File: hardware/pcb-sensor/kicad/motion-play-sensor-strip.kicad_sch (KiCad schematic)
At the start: 8 parts, among them J1 Power In, J2 Power Out, J3 I2C+INT, U1 VCNL4040M3OE-H3, U2 VCNL4040M3OE-H3

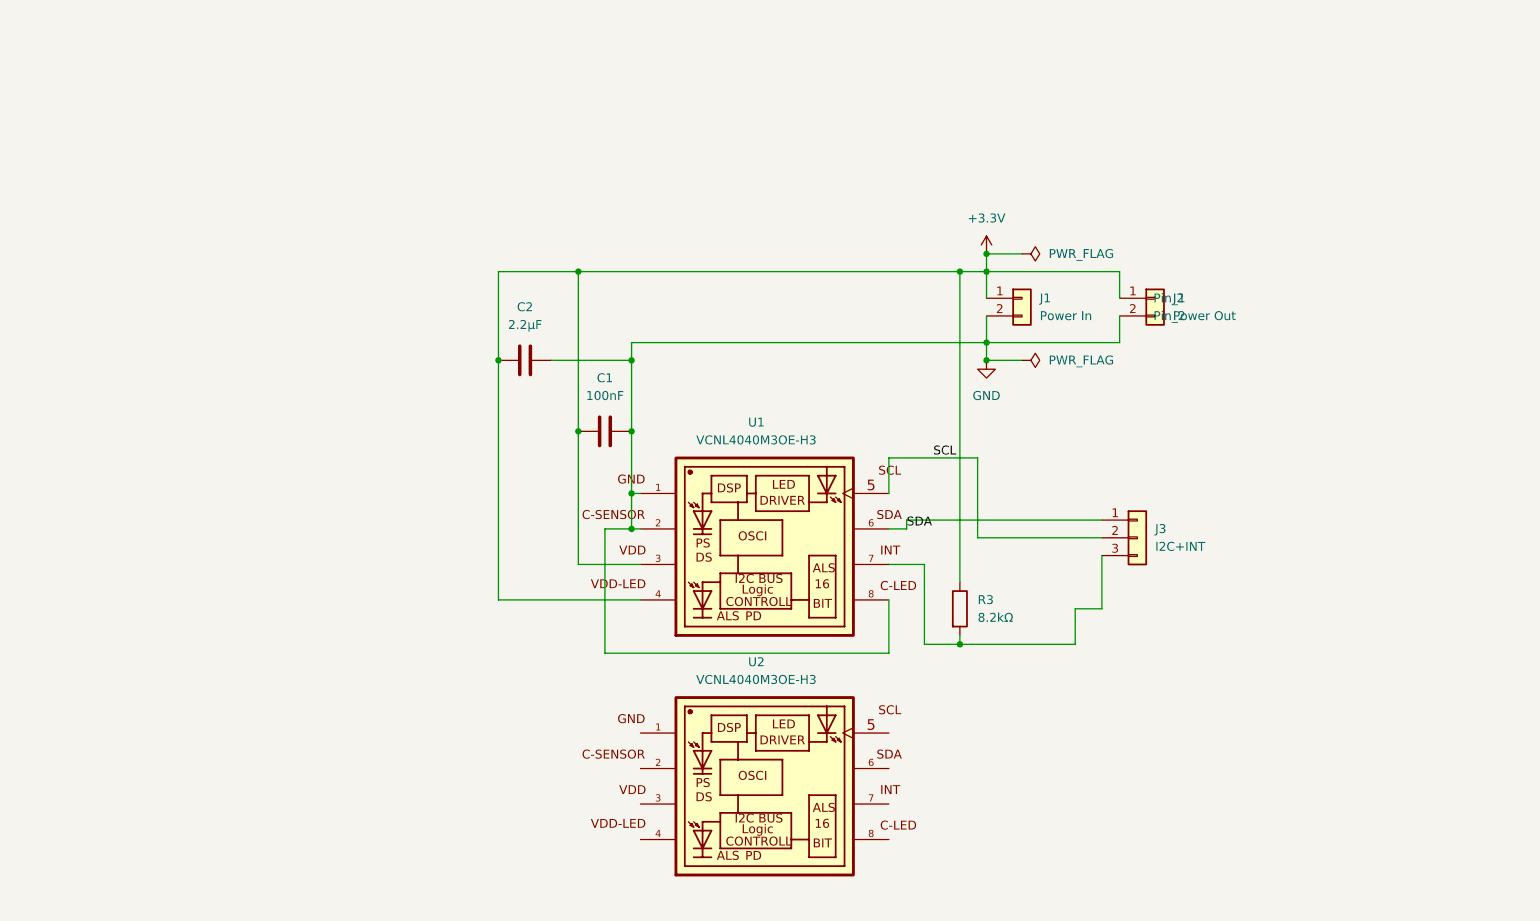
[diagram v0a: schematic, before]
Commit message: Finished sensor redesign
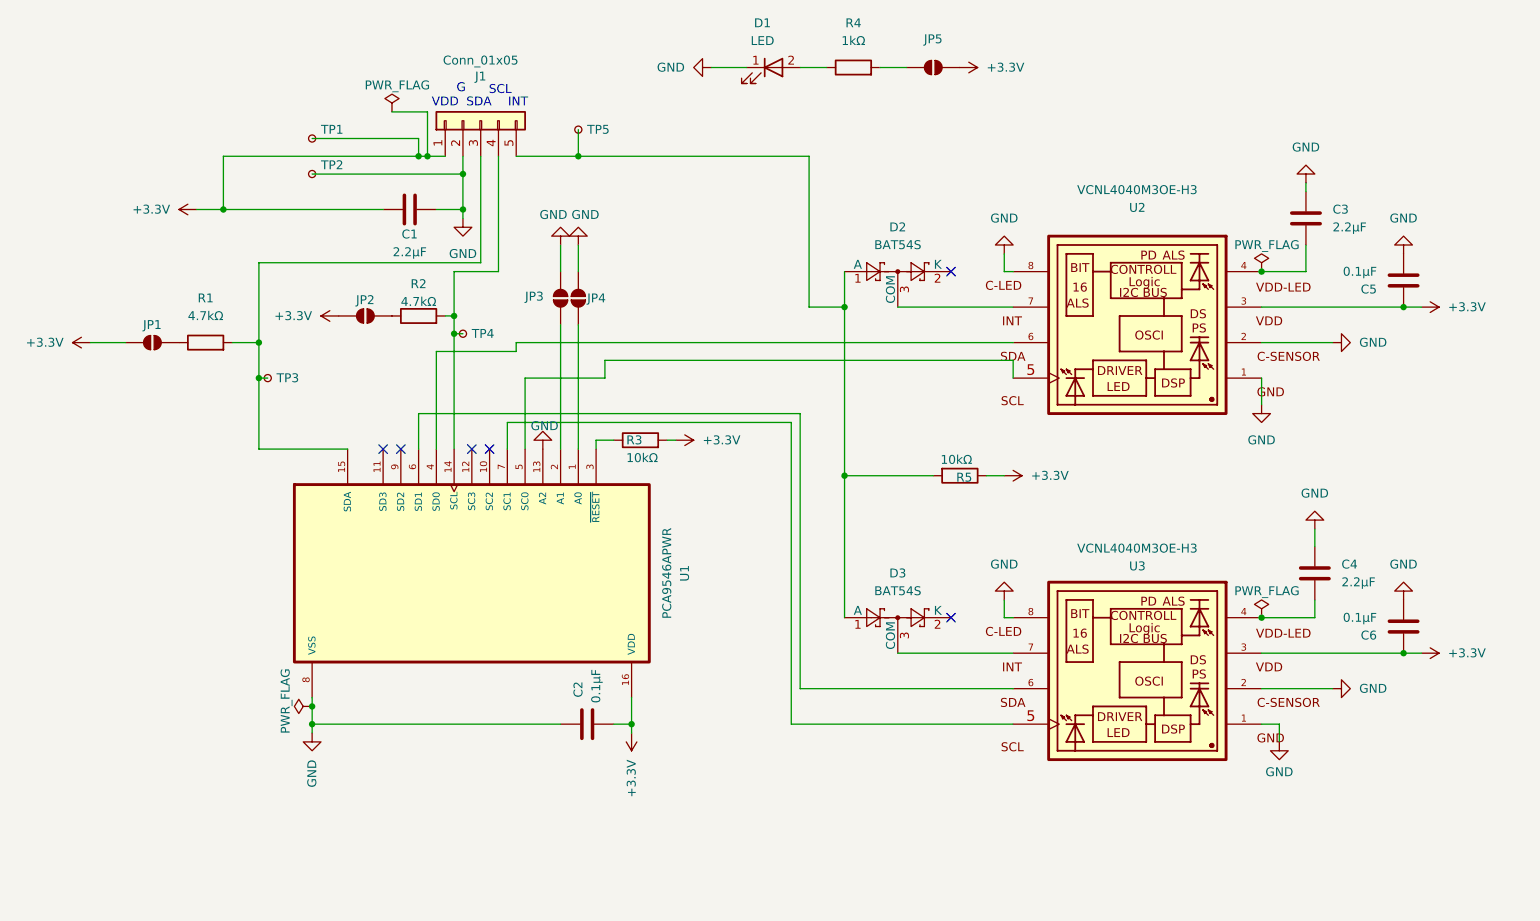
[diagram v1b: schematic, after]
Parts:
- removed J1: Power In, Connector_JST:JST_SH_SM02B-SRSS-TB_1x02-1MP_P1.00mm_Horizontal, symbol Connector_Generic:Conn_01x02
- removed J2: Power Out, Connector_JST:JST_SH_SM02B-SRSS-TB_1x02-1MP_P1.00mm_Horizontal, symbol Connector_Generic:Conn_01x02
- removed J3: I2C+INT, Connector_JST:JST_SH_SM03B-SRSS-TB_1x03-1MP_P1.00mm_Horizontal, symbol Connector_Generic:Conn_01x03
- added C3, C4: 2.2µF, Capacitor_SMD:C_0603_1608Metric, symbol Device:C
- added C5, C6: 0.1µF, Capacitor_SMD:C_0603_1608Metric, symbol Device:C
- added D1: LED, LED_SMD:LED_0603_1608Metric, symbol Device:LED
- added D2, D3: BAT54S, Package_TO_SOT_SMD:SOT-23, symbol Diode:BAT54S
- added J1: Conn_01x05, Connector_JST:JST_SH_SM05B-SRSS-TB_1x05-1MP_P1.00mm_Horizontal, symbol Connector_Generic:Conn_01x05
- added JP1, JP2, JP3, JP4, JP5: SolderJumper_2_Open, Jumper:SolderJumper-2_P1.3mm_Open_RoundedPad1.0x1.5mm, symbol Jumper:SolderJumper_2_Open
- added R1, R2: 4.7kΩ, Resistor_SMD:R_0603_1608Metric, symbol Device:R
- added R4: 1kΩ, Resistor_SMD:R_0603_1608Metric, symbol Device:R
- added R5: 10kΩ, Resistor_SMD:R_0603_1608Metric, symbol Device:R
- added TP1, TP2, TP3, TP4, TP5: TestPoint_Small, TestPoint:TestPoint_Pad_D1.5mm, symbol Connector:TestPoint_Small
- added U1: PCA9546APWR, motion-play-footprints:SOP65P640X120-16N, symbol motion-play-symbols:PCA9546APWR
- C1: value 100nF -> 2.2µF; LCSC Part C1590 -> C23630
- C2: value 2.2μF -> 0.1µF; LCSC Part C1607 -> C14663
- R3: value 8.2kΩ -> 10kΩ; LCSC Part C25981 -> C25804
- U2: renamed from U1; footprint VCNL4040:VISHAY_VCNL4040 -> motion-play-footprints:VISHAY_VCNL4040
- U3: renamed from U2; footprint VCNL4040:VISHAY_VCNL4040 -> motion-play-footprints:VISHAY_VCNL4040
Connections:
- net +3.3V: now also C1.2, C2.2, R3.2, U3.3, C5.1, C6.1, J1.1 (Pin_1), JP1.1 (A), JP2.1 (A), JP5.2 (B), R5.1, TP1.1, U1.16 (VDD); no longer C1.1, C2.1, R3.1, U2.4
- net GND: now also C1.1, C2.1, U3.1, U3.2, U3.8, C3.1, C4.1, C5.2, C6.2, D1.1 (K), J1.2 (Pin_2), JP3.2 (B), JP4.2 (B), TP2.1, U1.13 (A2), U1.8 (VSS); no longer C1.2, C2.2
- net at U3.4: now also C4.2
- net at U3.5: now also U1.7 (SC1)
- net at U3.6: now also U1.6 (SD1)
- net at U3.7: now also D3.3 (COM)
- net at U2.7: now also D2.3 (COM); no longer R3.2
- net SCL: no longer names the net of U2.5
- net SCL: now also U1.5 (SC0)
- net SDA: no longer names the net of U2.6
- net SDA: now also U1.4 (SD0)
- new net: JP2.2 (B), R2.1
- new net: J1.4 (Pin_4), R2.2, TP4.1, U1.14 (SCL)
- new net: C3.2, U2.4
- new net: J1.3 (Pin_3), R1.2, TP3.1, U1.15 (SDA)
- new net: D2.1 (A), D3.1 (A), J1.5 (Pin_5), R5.2, TP5.1
- new net: JP5.1 (A), R4.2
- new net: JP4.1 (A), U1.1 (A0)
- new net: JP3.1 (A), U1.2 (A1)
- new net: R3.1, U1.3 (~{RESET})
- new net: D1.2 (A), R4.1
- new net: JP1.2 (B), R1.1
- no-connect marks 0 -> 6
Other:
- note added: "G"
- note added: "INT"
- note added: "SCL"
- note added: "SDA"
- note added: "VDD"
- title: (none) -> Motion Play Sensor PCB
- moved on the sheet: U2, U3

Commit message: Proximity detection and updated pcbs
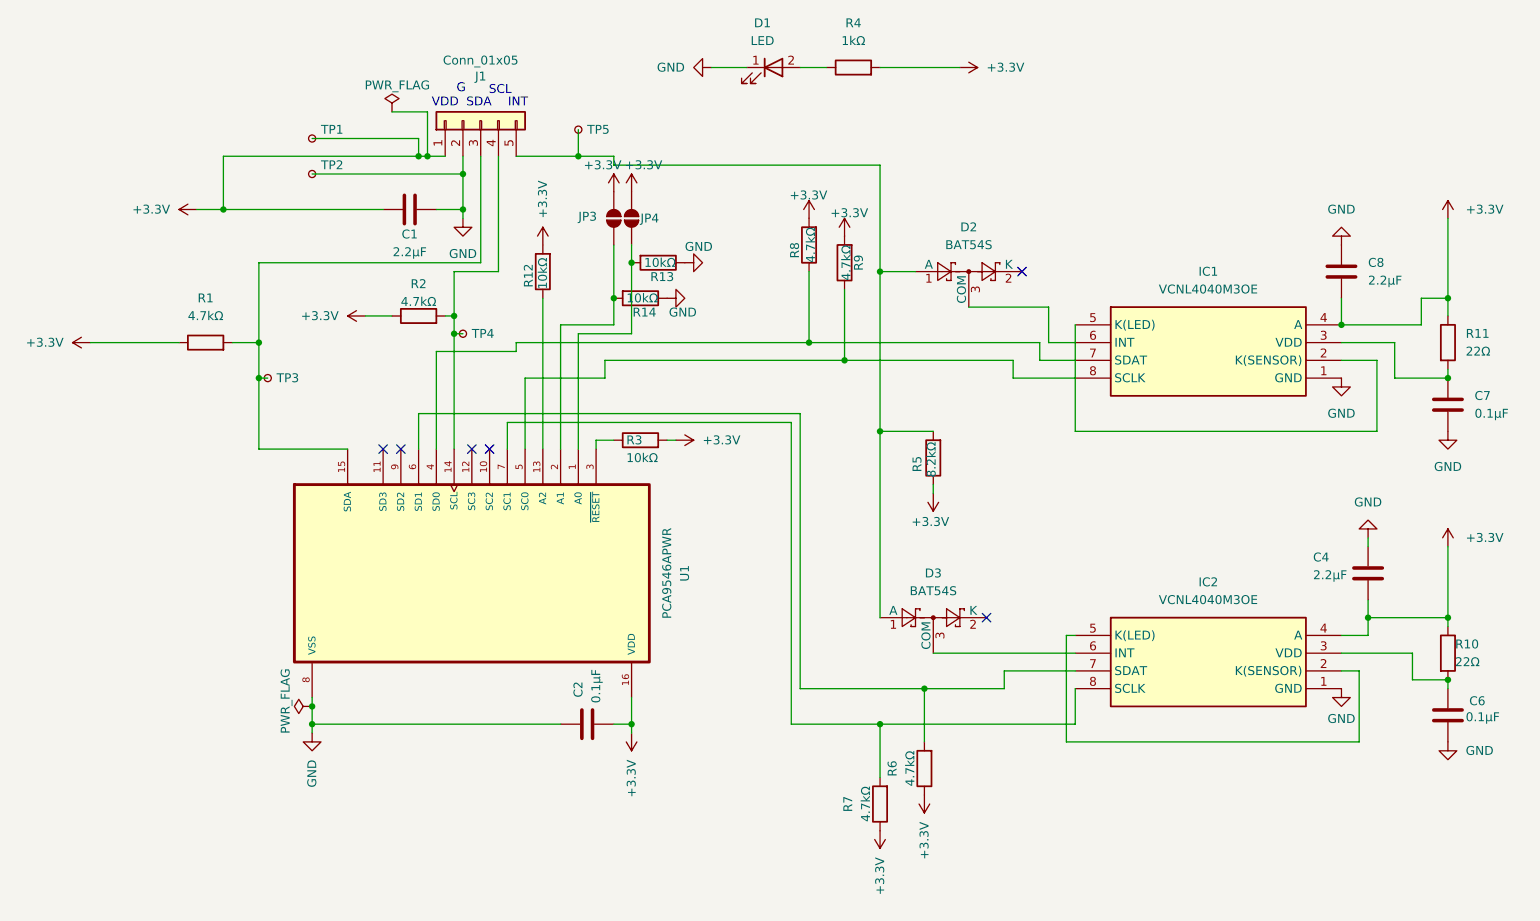
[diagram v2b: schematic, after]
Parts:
- removed C3: 2.2µF, Capacitor_SMD:C_0603_1608Metric, symbol Device:C
- removed C5: 0.1µF, Capacitor_SMD:C_0603_1608Metric, symbol Device:C
- removed JP1, JP2, JP5: SolderJumper_2_Open, Jumper:SolderJumper-2_P1.3mm_Open_RoundedPad1.0x1.5mm, symbol Jumper:SolderJumper_2_Open
- removed U2, U3: VCNL4040M3OE-H3, motion-play-footprints:VISHAY_VCNL4040, symbol VCNL4040:VCNL4040M3OE-H3
- added C7: 0.1µF, Capacitor_SMD:C_0603_1608Metric, symbol Device:C
- added C8: 2.2µF, Capacitor_SMD:C_0603_1608Metric, symbol Device:C
- added IC1, IC2: VCNL4040M3OE, motion-play-footprints:VCNL4040M3OE, symbol motion-play-symbols:VCNL4040M3OE
- added R10, R11: 22Ω, Resistor_SMD:R_0603_1608Metric, symbol Device:R
- added R12, R13, R14: 10kΩ, Resistor_SMD:R_0603_1608Metric, symbol Device:R
- added R6, R7, R8, R9: 4.7kΩ, Resistor_SMD:R_0603_1608Metric, symbol Device:R
- R5: value 10kΩ -> 8.2kΩ; LCSC Part C25804 -> C25981
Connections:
- net +3.3V: now also C4.2, JP3.2 (B), JP4.2 (B), R1.1, R2.1, R4.2, C8.2, IC1.4 (A), IC2.4 (A), R10.1, R11.1, R12.2, R6.1, R7.1, R8.2, R9.2; no longer C6.1
- net GND: now also C7.2, C8.1, IC1.1 (GND), IC2.1 (GND), R13.1, R14.1; no longer JP3.2 (B), JP4.2 (B), U1.13 (A2)
- net at U1.7 (SC1): now also IC2.8 (SCLK), R7.2
- net at U1.6 (SD1): now also IC2.7 (SDAT), R6.2
- net at D3.3 (COM): now also IC2.6 (INT)
- net at JP4.1 (A), U1.1 (A0): now also R13.2
- net at JP3.1 (A), U1.2 (A1): now also R14.2
- net at U1.4 (SD0): now also IC1.7 (SDAT), R8.1
- net at U1.5 (SC0): now also IC1.8 (SCLK), R9.1
- net at D2.3 (COM): now also IC1.6 (INT)
- new net: R12.1, U1.13 (A2)
- new net: C6.1, IC2.3 (VDD), R10.2
- new net: IC2.2 (K(SENSOR)), IC2.5 (K(LED))
- new net: C7.1, IC1.3 (VDD), R11.2
- new net: IC1.2 (K(SENSOR)), IC1.5 (K(LED))
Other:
- moved on the sheet: C4, C6, D2, D3, JP3, JP4, R5
